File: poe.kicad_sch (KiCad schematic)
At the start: 89 parts, among them Q1 FDMC2523P, Q2 FDMS86255, Q3 CSD17510Q5A, Q4 BCX56, Q5 CSD17510Q5A, T1 Transformer_Wurth_749119550, U20 TPS23734, U21 TCMT1107, U22 TL431CDBVR, U23 TCMT1107

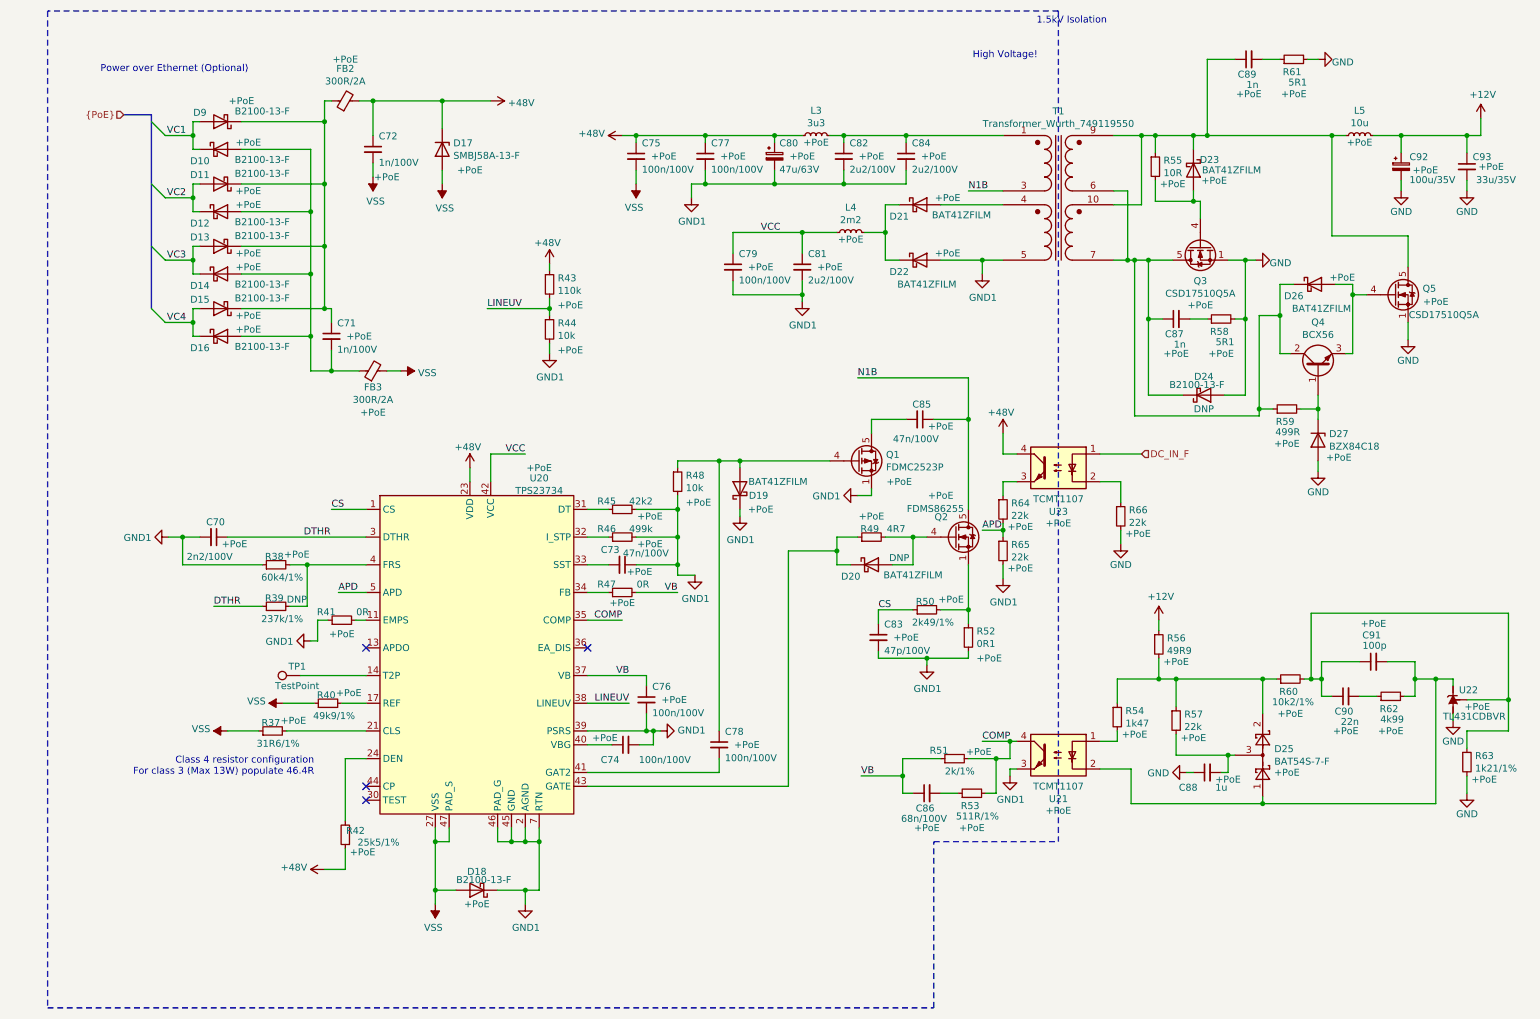
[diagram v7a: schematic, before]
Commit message: PoE: Migrate to opto-less feedback topology
Signed-off-by: Dominik Sliwa <dominik@sliwa.io>
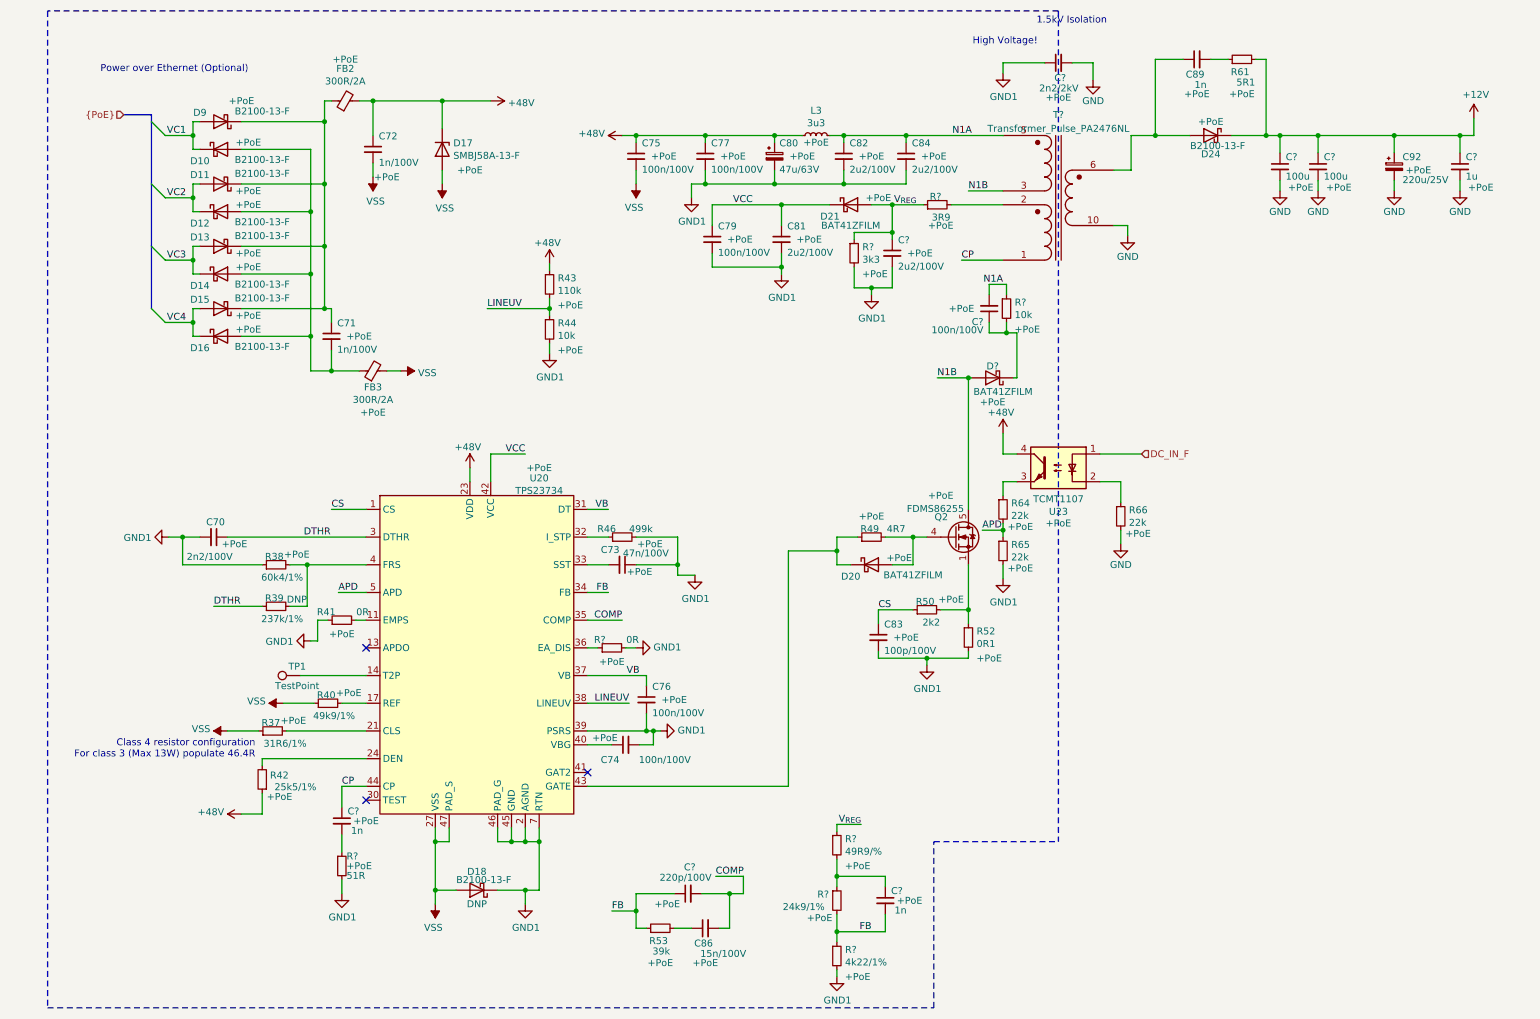
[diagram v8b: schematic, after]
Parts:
- removed C78: 100n/100V, Capacitor_SMD:C_0805_2012Metric, symbol Device:C_Small
- removed C85: 47n/100V, Capacitor_SMD:C_0805_2012Metric, symbol Device:C_Small
- removed C87: 1n, Capacitor_SMD:C_0402_1005Metric, symbol Device:C_Small
- removed C88: 1u, Capacitor_SMD:C_0402_1005Metric, symbol Device:C_Small
- removed C90: 22n, Capacitor_SMD:C_0402_1005Metric, symbol Device:C_Small
- removed C91: 100p, Capacitor_SMD:C_0402_1005Metric, symbol Device:C_Small
- removed C93: 33u/35V, Capacitor_Tantalum_SMD:CP_EIA-7343-31_Kemet-D, symbol Device:C_Small
- removed D19, D22, D23, D26: BAT41ZFILM, Diode_SMD:D_SOD-123, symbol Device:D_Schottky
- removed D25: BAT54S-7-F, Package_TO_SOT_SMD:SOT-23, symbol Diode:BAT54S
- removed D27: BZX84C18, Diode_SMD:D_SOT-23_ANK, symbol Diode:BZX84Cxx
- removed L4: 2m2, LightBlue:L_Bourns-SDR1006, symbol Device:L_Small
- removed L5: 10u, Inductor_SMD:L_Bourns_SRR1260, symbol Device:L_Small
- removed Q1: FDMC2523P, Package_SO:Vishay_PowerPAK_1212-8_Single, symbol Transistor_FET:SiS415DNT
- removed Q3, Q5: CSD17510Q5A, Package_TO_SOT_SMD:TDSON-8-1, symbol Transistor_FET:CSD17510Q5A
- removed Q4: BCX56, Package_TO_SOT_SMD:SOT-89-3, symbol Transistor_BJT:BCX56
- removed R45: 42k2, Resistor_SMD:R_0402_1005Metric, symbol Device:R_Small
- removed R47: 0R, Resistor_SMD:R_0402_1005Metric, symbol Device:R_Small
- removed R48: 10k, Resistor_SMD:R_0402_1005Metric, symbol Device:R_Small
- removed R51: 2k/1%, Resistor_SMD:R_0402_1005Metric, symbol Device:R_Small
- removed R54: 1k47, Resistor_SMD:R_0402_1005Metric, symbol Device:R_Small
- removed R55: 10R, Resistor_SMD:R_0402_1005Metric, symbol Device:R_Small
- removed R56: 49R9, Resistor_SMD:R_0402_1005Metric, symbol Device:R_Small
- removed R57: 22k, Resistor_SMD:R_0402_1005Metric, symbol Device:R_Small
- removed R58: 5R1, Resistor_SMD:R_0402_1005Metric, symbol Device:R_Small
- removed R59: 499R, Resistor_SMD:R_0402_1005Metric, symbol Device:R_Small
- removed R60: 10k2/1%, Resistor_SMD:R_0402_1005Metric, symbol Device:R_Small
- removed R62: 4k99, Resistor_SMD:R_0402_1005Metric, symbol Device:R_Small
- removed R63: 1k21/1%, Resistor_SMD:R_0402_1005Metric, symbol Device:R_Small
- removed T1: Transformer_Wurth_749119550, LightBlue:Transformer_Wuerth_749119550, symbol LightBlue:Transformer_Wurth_749119550
- removed U21: TCMT1107, Package_SO:SOP-4_4.4x2.6mm_P1.27mm, symbol Isolator:TCMT1107
- removed U22: TL431CDBVR, Package_TO_SOT_SMD:SOT-23-5, symbol Reference_Voltage:TL431DBV
- added C?: 220p/100V, Capacitor_SMD:C_0805_2012Metric, symbol Device:C_Small
- added C?: 1u, Capacitor_SMD:C_0402_1005Metric, symbol Device:C_Small
- added C? (x2): 1n, Capacitor_SMD:C_0402_1005Metric, symbol Device:C_Small
- added C?: 2n2/2kV, Capacitor_SMD:C_0402_1005Metric, symbol Device:C_Small
- added C? (x2): 100u, Capacitor_SMD:C_0402_1005Metric, symbol Device:C_Small
- added C?: 100n/100V, Capacitor_SMD:C_0805_2012Metric, symbol Device:C_Small
- added C?: 2u2/100V, Capacitor_SMD:C_0805_2012Metric, symbol Device:C_Small
- added D?: BAT41ZFILM, Diode_SMD:D_SOD-123, symbol Device:D_Schottky
- added R?: 10k, Resistor_SMD:R_0402_1005Metric, symbol Device:R_Small
- added R?: 51R, Resistor_SMD:R_0402_1005Metric, symbol Device:R_Small
- added R?: 3k3, Resistor_SMD:R_0402_1005Metric, symbol Device:R_Small
- added R?: 49R9/%, Resistor_SMD:R_0402_1005Metric, symbol Device:R_Small
- added R?: 24k9/1%, Resistor_SMD:R_0402_1005Metric, symbol Device:R_Small
- added R?: 0R, Resistor_SMD:R_0402_1005Metric, symbol Device:R_Small
- added R?: 4k22/1%, Resistor_SMD:R_0402_1005Metric, symbol Device:R_Small
- added R?: 3R9, Resistor_SMD:R_1206_3216Metric, symbol Device:R_Small
- added T?: Transformer_Pulse_PA2476NL, LightBlue:Transformer_EPQ-13, symbol LightBlue:Transformer_Pulse_PA2476NL
- C83: value 47p/100V -> 100p/100V
- C86: value 68n/100V -> 15n/100V
- C92: value 100u/35V -> 220u/25V
- D18: Config +PoE -> DNP
- D20, D24: Config DNP -> +PoE
- R50: value 2k49/1% -> 2k2
- R53: value 511R/1% -> 39k
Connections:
- net +12V: now also D24.1 (K), R61.2, C?.1, C?.1, C?.1
- net COMP: now also C86.2, C?.2; no longer R53.2
- net GND: now also C?.2, C?.2, C?.2, C?.2, T?.10 (N2B); no longer D24.2 (A), R61.2
- net GND1: now also C?.1, C?.2, R?.2, R?.2, R?.2, R?.2
- net N1B: now also D?.2 (A), T?.3 (N1B)
- net VB: now also U20.31 (DT); no longer C86.1
- net VCC: now also D21.1 (K)
- net N1A: now reaches C82.1, C84.1, L3.2
- net N1A: now also C?.2, R?.1, T?.5 (N1A)
- net FB: now reaches U20.34 (FB)
- net FB: now also R53.1, C?.1, C?.2, R?.1, R?.2
- net at U20.36 (EA_DIS): now also R?.1
- net CP: now reaches U20.44 (CP)
- net CP: now also C?.1, T?.1 (N4B)
- net at C89.1: now also D24.2 (A), T?.6 (N2A)
- net V_{REG}: now reaches D21.2 (A)
- net V_{REG}: now also C?.1, R?.1, R?.1, R?.1
- new net: C86.1, R53.2
- new net: C?.2, R?.1
- new net: C?.1, D?.1 (K), R?.2
- new net: C?.1, R?.1, R?.2
- new net: R?.2, T?.2 (N4A)
- no-connect marks 4 -> 3
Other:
- moved on the sheet: C79, C81, C86, C89, C92, D21, D24, R42, R53, R61
